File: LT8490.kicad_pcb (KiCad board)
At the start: 6 copper layers, 37.2 x 46 mm, 122 parts, among them J1 Conn_01x01, J10 Conn_01x01, J2 Conn_01x01, J3 Conn_01x01, J4 Conn_01x01, J5 Conn_01x01, J6 Conn_01x01, J7 Conn_01x01, J8 Conn_01x01, J9 Conn_01x01, Q1 Si7106DN, Q2 Si7106DN, Q3 Si7106DN, Q4 Si7106DN, Q5 BSS84, Q6 MBT2222ADW1T1, U4 LT8490EUKJPBF

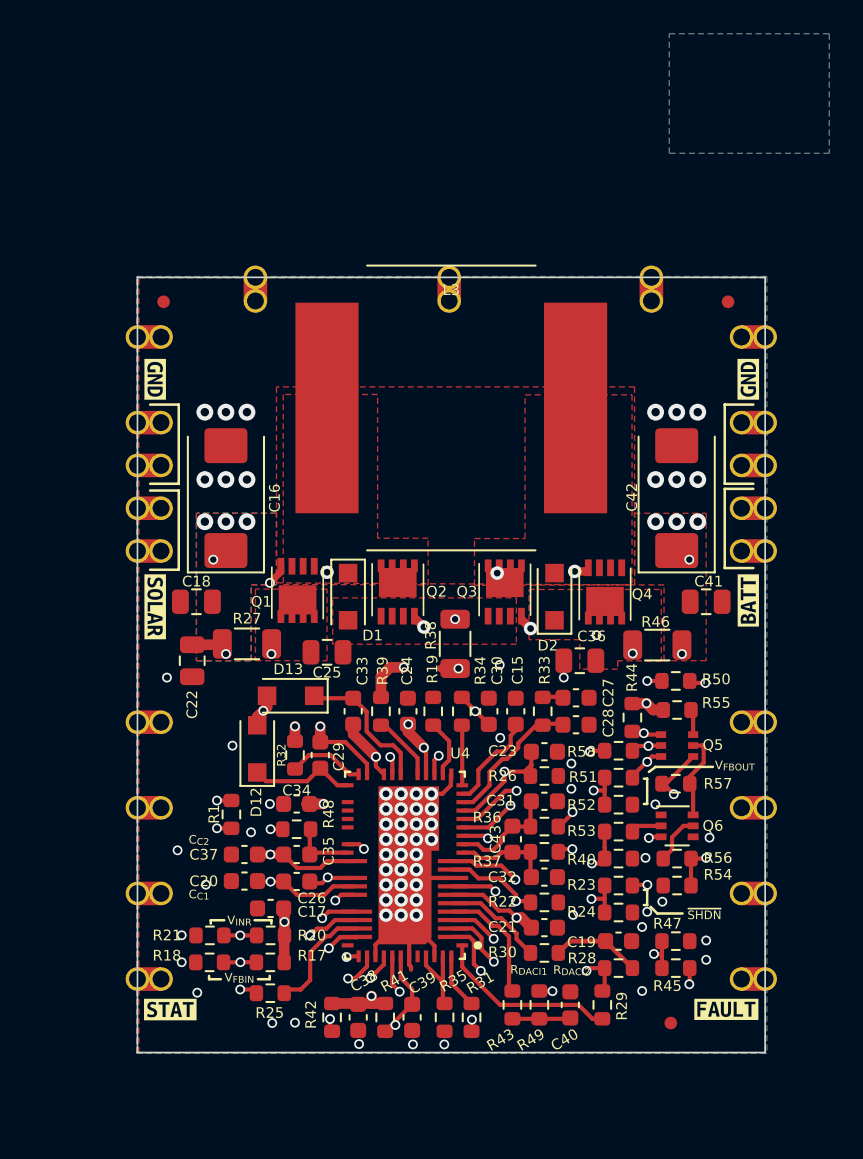
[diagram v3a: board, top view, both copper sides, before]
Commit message: passed DRC & extra SS labeling
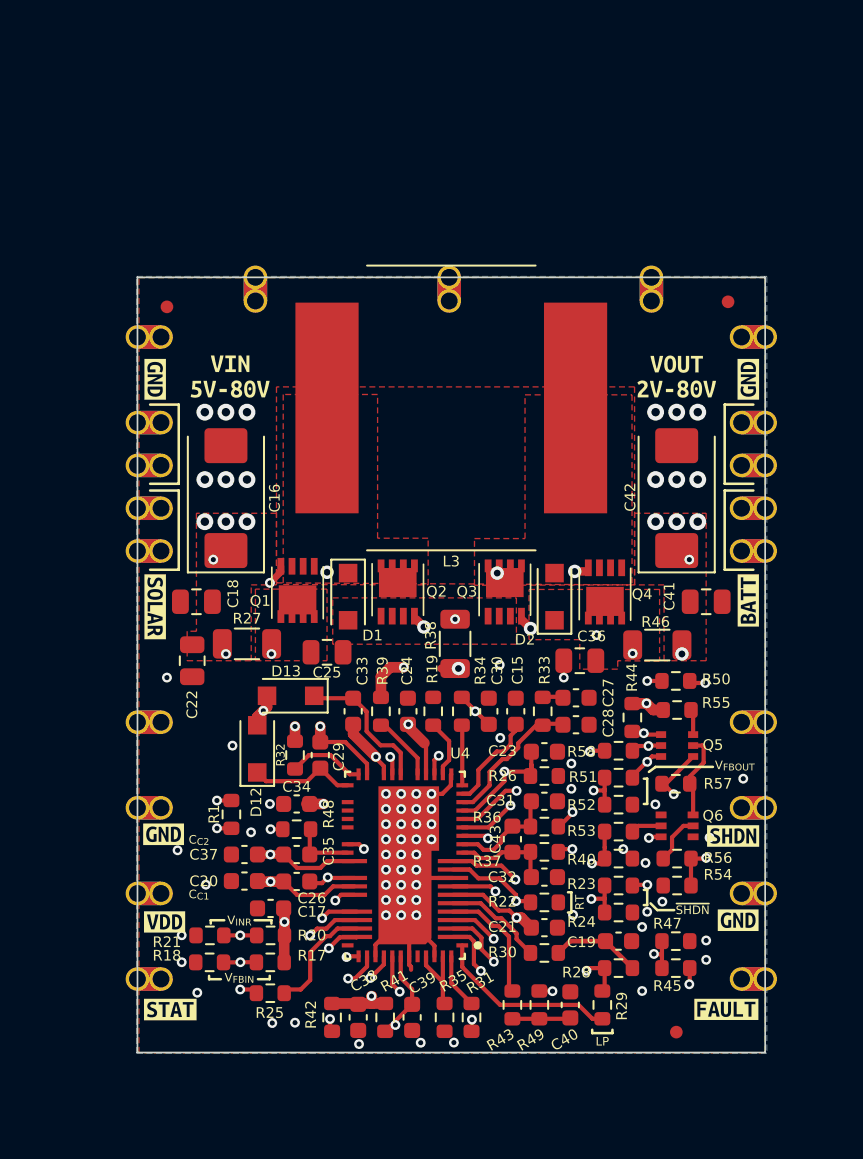
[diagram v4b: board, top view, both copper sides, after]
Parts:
- removed the REF** at (129.2, 79.3)
- removed the REF** at (166.5, 79.3)
- removed the REF** at (147.8, 75.8)
- removed the REF** at (136.2, 75.8)
- removed the REF** at (159.8, 75.8)
- removed REF**14, REF**15, REF**16, REF**5, REF**6, REF**7: castellated_05mm, custom-footprints:castellated_05mm
- added J11: Conn_01x01, custom-footprints:castellated_05mm, F.Cu at (130.7, 79.3)
- added J12: Conn_01x01, custom-footprints:castellated_05mm, F.Cu at (166.5, 79.3)
- added J13: Conn_01x01, custom-footprints:castellated_05mm, F.Cu at (130.7, 102.2)
- added J14: Conn_01x01, custom-footprints:castellated_05mm, F.Cu at (130.7, 107.2)
- added J15: Conn_01x01, custom-footprints:castellated_05mm, F.Cu at (130.7, 112.3)
- added J16: Conn_01x01, custom-footprints:castellated_05mm, F.Cu at (166.5, 102.2)
- added J17: Conn_01x01, custom-footprints:castellated_05mm, F.Cu at (166.5, 107.2)
- added J18: Conn_01x01, custom-footprints:castellated_05mm, F.Cu at (166.5, 112.3)
- added J19: Conn_01x01, custom-footprints:castellated_05mm, F.Cu at (136.2, 75.8)
- added J20: Conn_01x01, custom-footprints:castellated_05mm, F.Cu at (147.8, 75.8)
- added J21: Conn_01x01, custom-footprints:castellated_05mm, F.Cu at (159.8, 75.8)
- added kibuzzard-623CC1D5: G***, kibuzzard-623CC1D5, F.Cu at (164.9, 113.9)
- added kibuzzard-623CC1D5: G***, kibuzzard-623CC1D5, F.Cu at (130.8, 108.8)
- added kibuzzard-623CC9B2: G***, kibuzzard-623CC9B2, F.Cu at (130.9, 114.0)
- added kibuzzard-623CCAD0: G***, kibuzzard-623CCAD0, F.Cu at (134.8, 80.9)
- added kibuzzard-623CCAFA: G***, kibuzzard-623CCAFA, F.Cu at (134.8, 82.4)
- added kibuzzard-623CCB0B: G***, kibuzzard-623CCB0B, F.Cu at (161.2, 82.4)
- added kibuzzard-623CCB15: G***, kibuzzard-623CCB15, F.Cu at (161.2, 80.9)
- added kibuzzard-623CCD34: G***, kibuzzard-623CCD34, F.Cu at (164.6, 108.9)
- moved REF** 0.63 mm to (161.2, 120.5)
- moved REF** 0.36 mm to (131.0, 77.5)
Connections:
- net Net-(R23-Pad2) renamed /~{SHDN}
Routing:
- net Net-(NT1-Pad2): track 0.00 -> 18.2 mm, vias 0 -> 2
- net GND: track 26.2 -> 8.11 mm
- net V_{DD}: track 15.1 -> 30.1 mm
- net /CSNIN: track 0.00 -> 12.6 mm, vias 1 -> 2
- net Net-(C25-Pad1): track 11.8 -> 0.00 mm, vias 1 -> 0
- net /~{SHDN}: track 11.5 -> 22.7 mm
- net /CSPIN: track 24.7 -> 23.3 mm
- net GATEV_{CC}: vias 5 -> 4
- removed copper zone on B.Cu, net (none)
- removed copper zone on B.Cu, net VSOLAR
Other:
- board text added: "LP"
- board text added: "RT"
- board text removed: "R_{DACI1}"
- board text removed: "R_{DACI2}"

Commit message: Added LT8491 functionality (I2C)
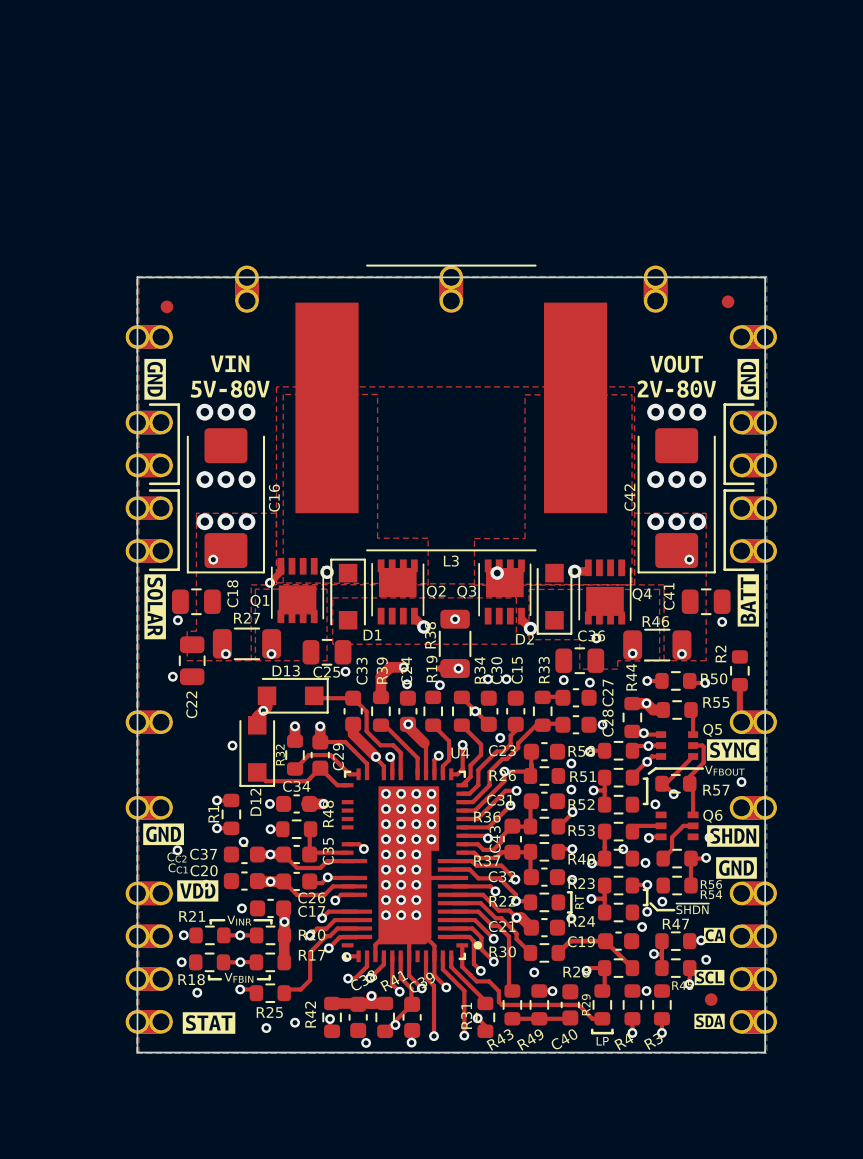
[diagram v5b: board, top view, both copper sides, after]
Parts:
- removed R35: 0, Resistor_SMD:R_0603_1608Metric
- removed kibuzzard-623CC40F: G***, kibuzzard-623CC40F
- added J22: Conn_01x01, custom-footprints:castellated_05mm, F.Cu at (166.5, 119.9)
- added J23: Conn_01x01, custom-footprints:castellated_05mm, F.Cu at (166.5, 117.4)
- added J24: Conn_01x01, custom-footprints:castellated_05mm, F.Cu at (130.7, 114.8)
- added J25: Conn_01x01, custom-footprints:castellated_05mm, F.Cu at (130.7, 119.9)
- added R2: 0, Resistor_SMD:R_0603_1608Metric, F.Cu at (165.0, 99.1)
- added R3: 0, Resistor_SMD:R_0603_1608Metric, F.Cu at (160.4, 118.9)
- added R4: 0, Resistor_SMD:R_0603_1608Metric, F.Cu at (158.6, 118.9)
- added kibuzzard-623DE3C4: G***, kibuzzard-623DE3C4, F.Cu at (164.6, 103.8)
- added kibuzzard-623E06E1: G***, kibuzzard-623E06E1, F.Cu at (163.5, 114.8)
- added kibuzzard-623E06ED: G***, kibuzzard-623E06ED, F.Cu at (163.2, 117.3)
- added kibuzzard-623E06FB: G***, kibuzzard-623E06FB, F.Cu at (163.2, 119.9)
- moved Ref** 3.26 mm to (138.1, 121.2)
- moved kibuzzard-623CC1D5 3.10 mm to (164.8, 110.8)
- moved REF** 2.83 mm to (163.3, 118.6)
- moved kibuzzard-623CC9B2 2.70 mm to (132.8, 112.2)
- moved J10 2.54 mm to (166.5, 114.8)
- moved kibuzzard-623CC3F2 2.44 mm to (133.5, 120.0)
- moved R31 0.82 mm to (149.9, 119.7)
- moved J19 0.50 mm to (135.8, 75.8)
- moved J21 0.25 mm to (160.0, 75.8)
- moved J20 0.12 mm to (147.9, 75.8)
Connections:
- J16 pad 1: unconnected-(J16-Pad1) -> /SYNC
- J9 pad 1: REG_{STATUS} -> unconnected-(J9-Pad1)
- U4 pad 21: GND -> /SYNC
- U4 pad 61: Net-(R35-Pad1) -> /SDA
- U4 pad 63: Net-(R35-Pad1) -> /SCL
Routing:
- net VBATT: track 0.00 -> 41.5 mm, vias 3 -> 5
- net /CSNOUT: track 41.5 -> 0.00 mm, vias 2 -> 0
- net /SYNC: track 0.00 -> 28.6 mm, vias 0 -> 1
- net /SDA: track 0.00 -> 24.9 mm, vias 0 -> 2
- net /SCL: track 0.00 -> 24.0 mm, vias 0 -> 2
- net Net-(R35-Pad1): track 5.23 -> 0.00 mm
- net GATEV_{CC}: track 38.5 -> 40.6 mm
- net GND: track 8.11 -> 9.60 mm, vias 70 -> 82
- net REG_{STATUS}: track 17.5 -> 16.4 mm
- net Net-(R34-Pad2): track 3.58 -> 4.50 mm
- net Net-(C23-Pad1): track 40.0 -> 40.6 mm
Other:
- rule pad_to_mask_clearance: 0.0508 -> 0

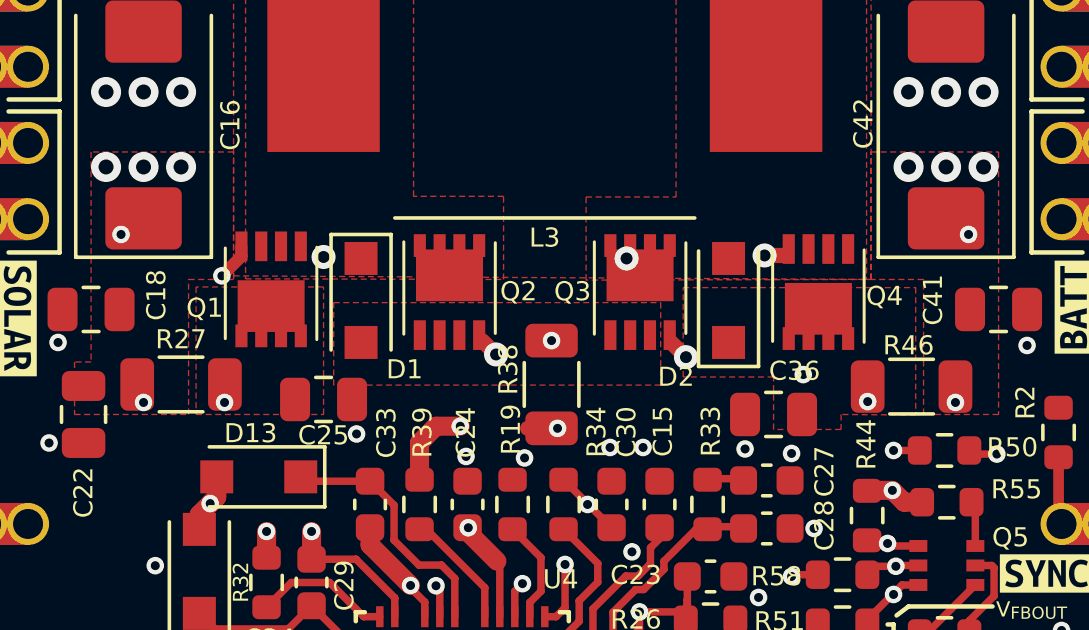
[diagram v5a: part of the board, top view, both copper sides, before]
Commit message: Added module highlights and part justifications to readme
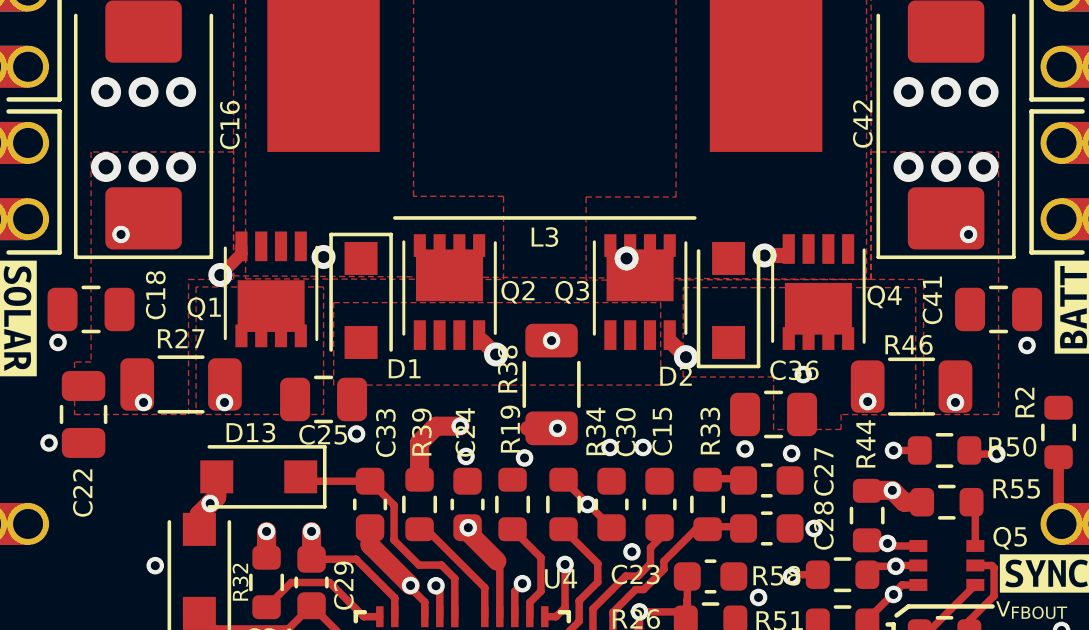
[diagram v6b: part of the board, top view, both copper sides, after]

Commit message: pin labels for schematic and layout blocks
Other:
- board text added: "1"
- board text added: "10"
- board text added: "11"
- board text added: "12"
- board text added: "13"
- board text added: "14"
- board text added: "2"
- board text added: "3"
- board text added: "4"
- board text added: "5"
- board text added: "6"
- board text added: "7"
- board text added: "8"
- board text added: "9"
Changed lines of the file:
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@@
     (effects (font (size 0.508 0.508) (thickness 0.1016)))
+  )
+  (gr_text "1" (at 127 120) (layer "Cmts.User")
+    (effects (font (size 1 1) (thickness 0.15)))
+  )
+  (gr_text "5" (at 127 84.582) (layer "Cmts.User")
+    (effects (font (size 1 1) (thickness 0.15)))
+  )
+  (gr_text "5" (at 127 107.188) (layer "Cmts.User")
+    (effects (font (size 1 1) (thickness 0.15)))
+  )
+  (gr_text "9" (at 168.91 89.408) (layer "Cmts.User")
+    (effects (font (size 1 1) (thickness 0.15)))
+  )
+  (gr_text "5" (at 168.91 84.328) (layer "Cmts.User")
+    (effects (font (size 1 1) (thickness 0.15)))
+  )
+  (gr_text "4" (at 127 112.268) (layer "Cmts.User")
+    (effects (font (size 1 1) (thickness 0.15)))
+  )
+  (gr_text "2" (at 127 117.348) (layer "Cmts.User")
+    (effects (font (size 1 1) (thickness 0.15)))
+  )
+  (gr_text "11" (at 168.91 107.188) (layer "Cmts.User")
+    (effects (font (size 1 1) (thickness 0.15)))
+  )
+  (gr_text "3" (at 127 114.808) (layer "Cmts.User")
+    (effects (font (size 1 1) (thickness 0.15)))
+  )
+  (gr_text "7" (at 127 89.408) (layer "Cmts.User")
+    (effects (font (size 1 1) (thickness 0.15)))
+  )
+  (gr_text "5" (at 168.91 86.868) (layer "Cmts.User")
+    (effects (font (size 1 1) (thickness 0.15)))
+  )
+  (gr_text "9" (at 168.91 91.948) (layer "Cmts.User")
+    (effects (font (size 1 1) (thickness 0.15)))
+  )
+  (gr_text "10" (at 168.91 102.108) (layer "Cmts.User")
+    (effects (font (size 1 1) (thickness 0.15)))
+  )
+  (gr_text "6" (at 127 102.108) (layer "Cmts.User")
+    (effects (font (size 1 1) (thickness 0.15)))
+  )
+  (gr_text "5" (at 135.636 73.66) (layer "Cmts.User")
+    (effects (font (size 1 1) (thickness 0.15)))
+  )
+  (gr_text "5" (at 160.02 73.66) (layer "Cmts.User")
+    (effects (font (size 1 1) (thickness 0.15)))
+  )
+  (gr_text "5" (at 127 79.248) (layer "Cmts.User")
+    (effects (font (size 1 1) (thickness 0.15)))
+  )
+  (gr_text "5" (at 168.91 112.268) (layer "Cmts.User")
+    (effects (font (size 1 1) (thickness 0.15)))
+  )
+  (gr_text "5" (at 127 86.868) (layer "Cmts.User")
+    (effects (font (size 1 1) (thickness 0.15)))
+  )
+  (gr_text "5" (at 168.91 79.248) (layer "Cmts.User")
+    (effects (font (size 1 1) (thickness 0.15)))
+  )
+  (gr_text "12" (at 168.91 114.808) (layer "Cmts.User")
+    (effects (font (size 1 1) (thickness 0.15)))
+  )
+  (gr_text "8" (at 147.828 73.914) (layer "Cmts.User")
+    (effects (font (size 1 1) (thickness 0.15)))
+  )
+  (gr_text "14" (at 168.91 119.888) (layer "Cmts.User")
+    (effects (font (size 1 1) (thickness 0.15)))
+  )
+  (gr_text "7" (at 127 92.202) (layer "Cmts.User")
+    (effects (font (size 1 1) (thickness 0.15)))
+  )
+  (gr_text "13" (at 168.91 117.348) (layer "Cmts.User")
+    (effects (font (size 1 1) (thickness 0.15)))
   )
   (dimension (type aligned) (layer "Dwgs.User")
